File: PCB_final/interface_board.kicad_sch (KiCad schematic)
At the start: 116 parts, among them J1 02x30_Shift_Register_Connector, J2 02x30_ADC_Connector, J5 PicoPinSocketB, J6 PicoPinSocketA, U1 74HC595, U10 LM321, U2 74HC595, U3 74HC595, U4 74HC595, U5 74HC595, U6 74HC595, U7 74HC595, U8 MAX11643EEG, U9 MAX11643EEG

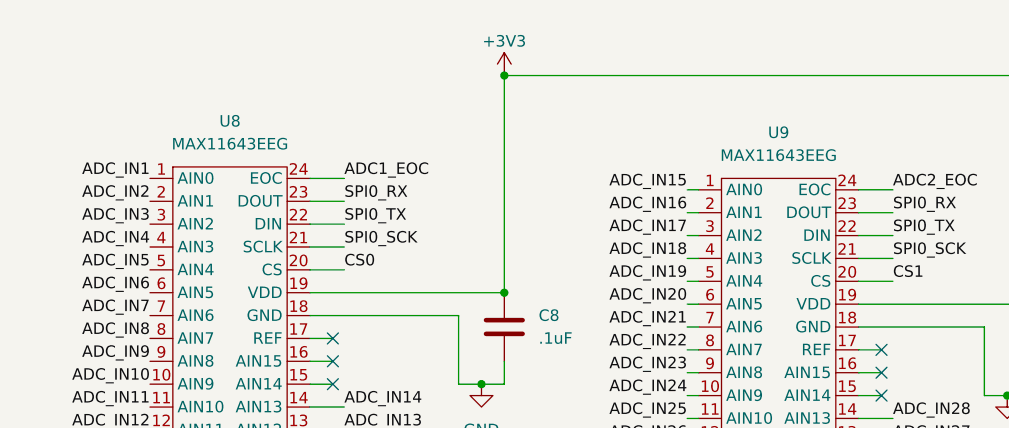
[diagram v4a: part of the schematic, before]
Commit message: Added footprints to the ADCS
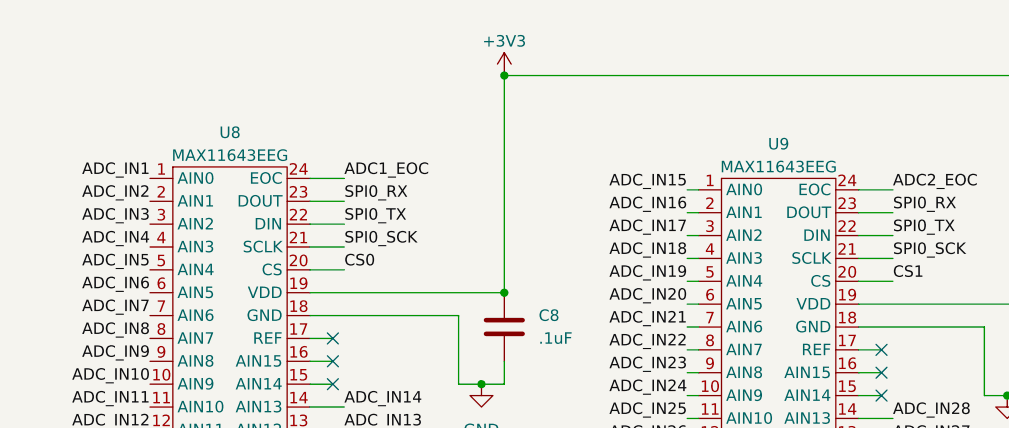
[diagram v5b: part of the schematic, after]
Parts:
- U8, U9: footprint (none) -> Package_SO:SSOP-24_3.9x8.7mm_P0.635mm
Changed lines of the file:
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@@
     )
   )
+  (symbol (lib_id "Capstone_Library:MAX11643EEG") (at 248.92 46.99 0) (unit 1)
+    (in_bom yes) (on_board yes) (dnp no)
+    (property "Reference" "U9" (at 248.92 27.94 0)
+      (effects (font (size 1.27 1.27)))
+    )
+    (property "Value" "MAX11643EEG" (at 248.92 30.48 0)
+      (effects (font (size 1.27 1.27)))
+    )
+    (property "Footprint" "Package_SO:SSOP-24_3.9x8.7mm_P0.635mm" (at 240.03 33.02 0)
+      (effects (font (size 1.27 1.27)) hide)
+    )
+    (property "Datasheet" "" (at 240.03 33.02 0) (do_not_autoplace)
+      (effects (font (size 1.27 1.27)) hide)
+    )
+    (pin "1")
+    (pin "10")
+    (pin "11")
+    (pin "12")
+    (pin "13")
+    (pin "14")
+    (pin "15")
+    (pin "16")
+    (pin "17")
+    (pin "18")
+    (pin "19")
+    (pin "2")
+    (pin "20")
+    (pin "21")
+    (pin "22")
+    (pin "23")
+    (pin "3")
+    (pin "4")
+    (pin "5")
+    (pin "6")
+    (pin "7")
+    (pin "8")
+    (pin "9")
+    (pin "24")
+    (instances
+      (project "PCB_final"
+        (path "/e4192969-4b4c-4bbf-a0a8-ef09d84e64d7/e0559890-1aa0-4336-9a3e-110d23fe279d"
+          (reference "U9") (unit 1)
+        )
+      )
+    )
+  )
   (symbol (lib_id "power:GND") (at 193.04 148.59 0) (unit 1)
     (in_bom yes) (on_board yes) (dnp no)
@@
     )
   )
+  (symbol (lib_name "MAX11643EEG_1") (lib_id "Capstone_Library:MAX11643EEG") (at 187.96 45.72 0) (unit 1)
+    (in_bom yes) (on_board yes) (dnp no)
+    (property "Reference" "U8" (at 187.96 26.67 0)
+      (effects (font (size 1.27 1.27)))
+    )
+    (property "Value" "MAX11643EEG" (at 187.96 29.21 0)
+      (effects (font (size 1.27 1.27)))
+    )
+    (property "Footprint" "Package_SO:SSOP-24_3.9x8.7mm_P0.635mm" (at 179.07 31.75 0)
+      (effects (font (size 1.27 1.27)) hide)
+    )
+    (property "Datasheet" "" (at 179.07 31.75 0) (do_not_autoplace)
+      (effects (font (size 1.27 1.27)) hide)
+    )
+    (pin "1")
+    (pin "10")
+    (pin "11")
+    (pin "12")
+    (pin "13")
+    (pin "14")
+    (pin "15")
+    (pin "16")
+    (pin "17")
+    (pin "18")
+    (pin "19")
+    (pin "2")
+    (pin "20")
+    (pin "21")
+    (pin "22")
+    (pin "23")
+    (pin "3")
+    (pin "4")
+    (pin "5")
+    (pin "6")
+    (pin "7")
+    (pin "8")
+    (pin "9")
+    (pin "24")
+    (instances
+      (project "PCB_final"
+        (path "/e4192969-4b4c-4bbf-a0a8-ef09d84e64d7/e0559890-1aa0-4336-9a3e-110d23fe279d"
+          (reference "U8") (unit 1)
+        )
+      )
+    )
+  )
   (symbol (lib_id "power:+3V3") (at 81.28 59.69 0) (unit 1)
     (in_bom yes) (on_board yes) (dnp no)
@@
     )
   )
-  (symbol (lib_id "Capstone_Library:MAX11643EEG") (at 187.96 45.72 0) (unit 1)
-    (in_bom yes) (on_board yes) (dnp no)
-    (property "Reference" "U8" (at 187.96 25.4 0)
-      (effects (font (size 1.27 1.27)))
-    )
-    (property "Value" "MAX11643EEG" (at 187.96 27.94 0)
-      (effects (font (size 1.27 1.27)))
-    )
-    (property "Footprint" "" (at 179.07 31.75 0)
-      (effects (font (size 1.27 1.27)) hide)
-    )
-    (property "Datasheet" "" (at 179.07 31.75 0) (do_not_autoplace)
-      (effects (font (size 1.27 1.27)) hide)
-    )
-    (property "Evan Desmond" "" (at 187.96 45.72 0)
-      (effects (font (size 1.27 1.27)) hide)
-    )
-    (pin "1")
-    (pin "10")
-    (pin "11")
-    (pin "12")
-    (pin "13")
-    (pin "14")
-    (pin "15")
-    (pin "16")
-    (pin "17")
-    (pin "18")
-    (pin "19")
-    (pin "2")
-    (pin "20")
-    (pin "21")
-    (pin "22")
-    (pin "23")
-    (pin "3")
-    (pin "4")
-    (pin "5")
-    (pin "6")
-    (pin "7")
-    (pin "8")
-    (pin "9")
-    (pin "24")
-    (instances
-      (project "PCB_final"
-        (path "/e4192969-4b4c-4bbf-a0a8-ef09d84e64d7"
-          (reference "U8") (unit 1)
-        )
-        (path "/e4192969-4b4c-4bbf-a0a8-ef09d84e64d7/e0559890-1aa0-4336-9a3e-110d23fe279d"
-          (reference "U8") (unit 1)
-        )
-      )
-    )
-  )
   (symbol (lib_id "Diode:MMSD4148") (at 127 26.67 180) (unit 1)
     (in_bom yes) (on_board yes) (dnp no)
@@
         )
       )
-    )
-  )
-  (symbol (lib_id "Capstone_Library:MAX11643EEG") (at 248.92 46.99 0) (unit 1)
-    (in_bom yes) (on_board yes) (dnp no)
-    (property "Reference" "U9" (at 248.92 26.67 0)
-      (effects (font (size 1.27 1.27)))
-    )
-    (property "Value" "MAX11643EEG" (at 248.92 29.21 0)
-      (effects (font (size 1.27 1.27)))
-    )
-    (property "Footprint" "" (at 240.03 33.02 0)
-      (effects (font (size 1.27 1.27)) hide)
-    )
-    (property "Datasheet" "" (at 240.03 33.02 0) (do_not_autoplace)
-      (effects (font (size 1.27 1.27)) hide)
-    )
-    (property "Evan Desmond" "" (at 248.92 46.99 0)
-      (effects (font (size 1.27 1.27)) hide)
-    )
-    (pin "1")
-    (pin "10")
-    (pin "11")
-    (pin "12")
-    (pin "13")
-    (pin "14")
-    (pin "15")
-    (pin "16")
-    (pin "17")
-    (pin "18")
-    (pin "19")
-    (pin "2")
-    (pin "20")
-    (pin "21")
-    (pin "22")
-    (pin "23")
-    (pin "3")
-    (pin "4")
-    (pin "5")
-    (pin "6")
-    (pin "7")
-    (pin "8")
-    (pin "9")
-    (pin "24")
-    (instances
-      (project "PCB_final"
-        (path "/e4192969-4b4c-4bbf-a0a8-ef09d84e64d7"
-          (reference "U9") (unit 1)
-        )
-        (path "/e4192969-4b4c-4bbf-a0a8-ef09d84e64d7/e0559890-1aa0-4336-9a3e-110d23fe279d"
-          (reference "U9") (unit 1)
-        )
-      )

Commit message: Added footprints to all components
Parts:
- C1, C10, C2, C8: footprint (none) -> Capacitor_SMD:C_0603_1608Metric
- J1, J2: footprint (none) -> Connector_PinHeader_2.54mm:PinHeader_2x30_P2.54mm_Vertical
- J6: footprint (none) -> Connector_PinSocket_2.54mm:PinSocket_1x20_P2.54mm_Vertical
- R1, R2, R3: footprint (none) -> Resistor_SMD:R_0603_1608Metric
- U1, U2, U3, U4, U5, U6, U7: footprint (none) -> Package_DIP:DIP-16_W7.62mm

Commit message: nearly finished with pcb routing
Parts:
- J5: footprint (none) -> Connector_PinSocket_2.54mm:PinSocket_1x20_P2.54mm_Vertical
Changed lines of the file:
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@@
       (effects (font (size 1.27 1.27)) (justify left))
     )
-    (property "Footprint" "" (at 255.27 113.03 0)
+    (property "Footprint" "Connector_PinSocket_2.54mm:PinSocket_1x20_P2.54mm_Vertical" (at 255.27 113.03 0)
       (effects (font (size 1.27 1.27)) hide)
     )

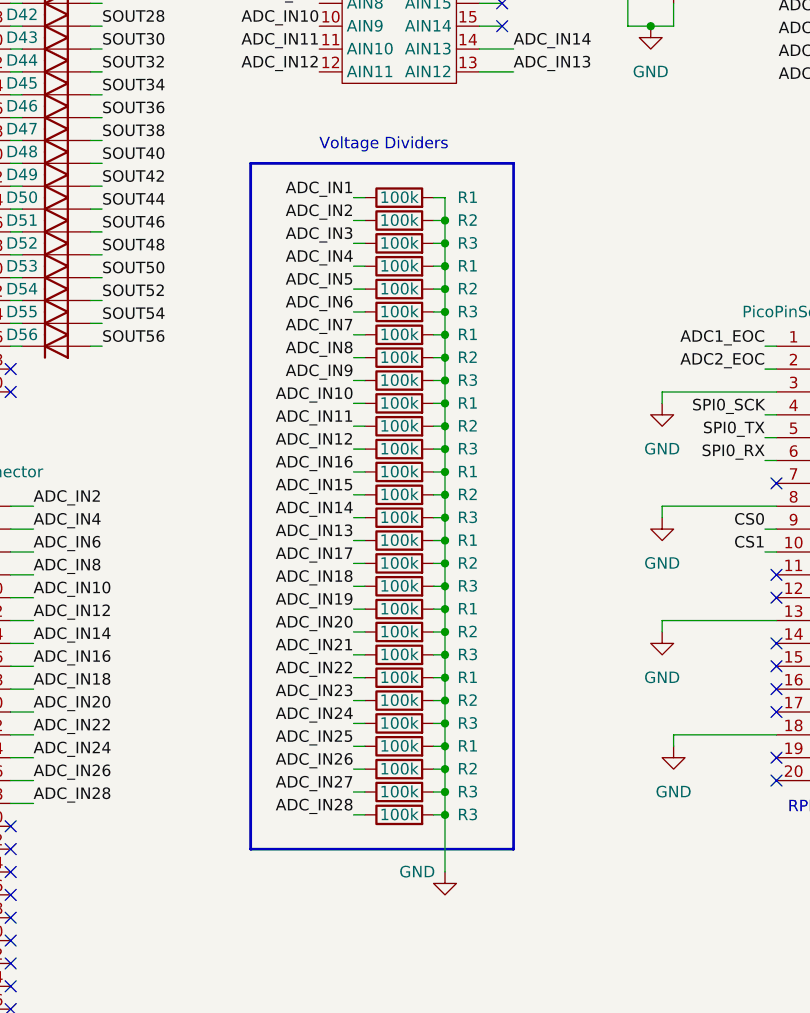
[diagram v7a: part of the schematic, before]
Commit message: Swapped resistors on schematic from european to US
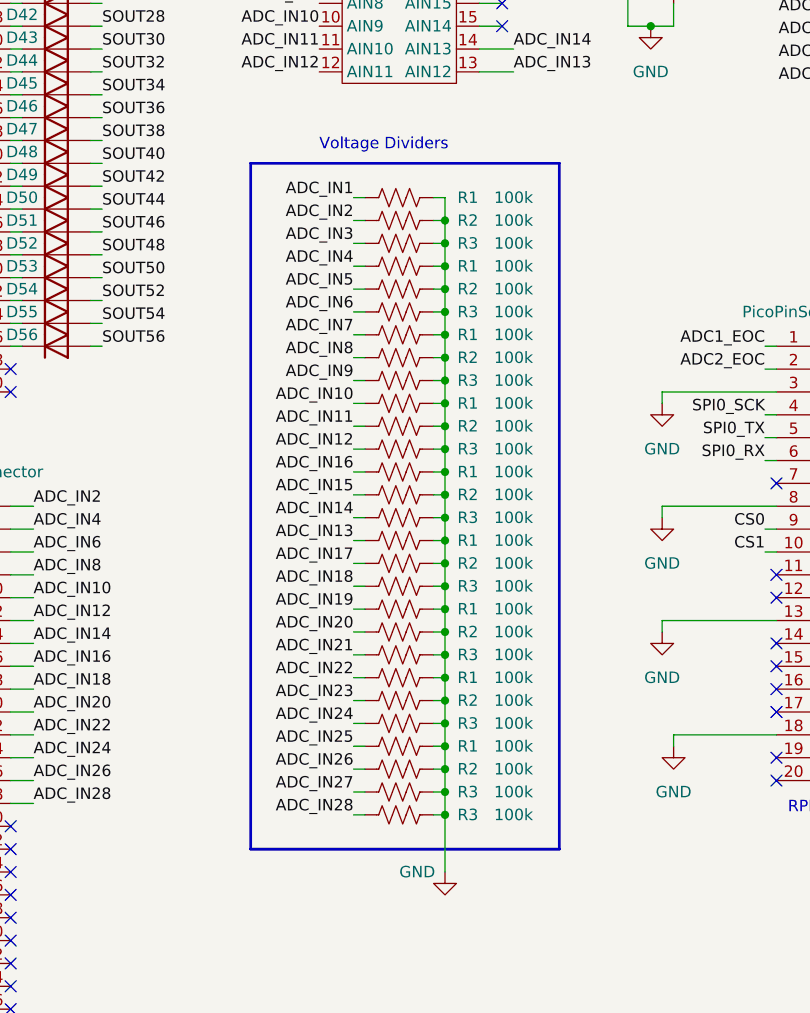
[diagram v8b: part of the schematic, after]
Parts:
- R1, R2, R3: symbol Device:R -> Device:R_US
